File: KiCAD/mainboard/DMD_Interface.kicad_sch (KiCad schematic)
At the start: 21 parts, among them IC3 SN74AUP1G06DCKR, IC4 SN74AUP1G07DCKR, IC5 SN74AUP1G07DCKR, J1 AXT550124, J10 Conn_01x05_Pin, J30 Conn_01x08_Pin

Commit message: some new schematics
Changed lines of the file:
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@@
 	(rectangle
 		(start 17.145 58.42)
-		(end 104.775 167.005)
+		(end 104.775 185.42)
 		(stroke
 			(width 0)
@@
 		)
 		(instances
-			(project ""
+			(project "mainboard"
 				(path "/38e83f42-2cf9-4799-a46f-ca415d95b90a/2ef4843e-e813-4038-8f91-df837a4944f8"
 					(reference "J1")
@@
 		)
 		(instances
-			(project ""
+			(project "mainboard"
 				(path "/38e83f42-2cf9-4799-a46f-ca415d95b90a/2ef4843e-e813-4038-8f91-df837a4944f8"
 					(reference "D6")
@@
 		)
 		(instances
-			(project ""
+			(project "mainboard"
 				(path "/38e83f42-2cf9-4799-a46f-ca415d95b90a/2ef4843e-e813-4038-8f91-df837a4944f8"
 					(reference "IC4")
@@
 		)
 		(instances
-			(project ""
+			(project "mainboard"
 				(path "/38e83f42-2cf9-4799-a46f-ca415d95b90a/2ef4843e-e813-4038-8f91-df837a4944f8"
 					(reference "C116")
@@
 		)
 		(instances
-			(project ""
+			(project "mainboard"
 				(path "/38e83f42-2cf9-4799-a46f-ca415d95b90a/2ef4843e-e813-4038-8f91-df837a4944f8"
 					(reference "#PWR02")
@@
 		)
 		(instances
-			(project ""
+			(project "mainboard"
 				(path "/38e83f42-2cf9-4799-a46f-ca415d95b90a/2ef4843e-e813-4038-8f91-df837a4944f8"
 					(reference "IC3")
@@
 		)
 		(instances
-			(project ""
+			(project "mainboard"
 				(path "/38e83f42-2cf9-4799-a46f-ca415d95b90a/2ef4843e-e813-4038-8f91-df837a4944f8"
 					(reference "#PWR01")
@@
 		)
 		(instances
-			(project ""
+			(project "mainboard"
 				(path "/38e83f42-2cf9-4799-a46f-ca415d95b90a/2ef4843e-e813-4038-8f91-df837a4944f8"
 					(reference "J30")

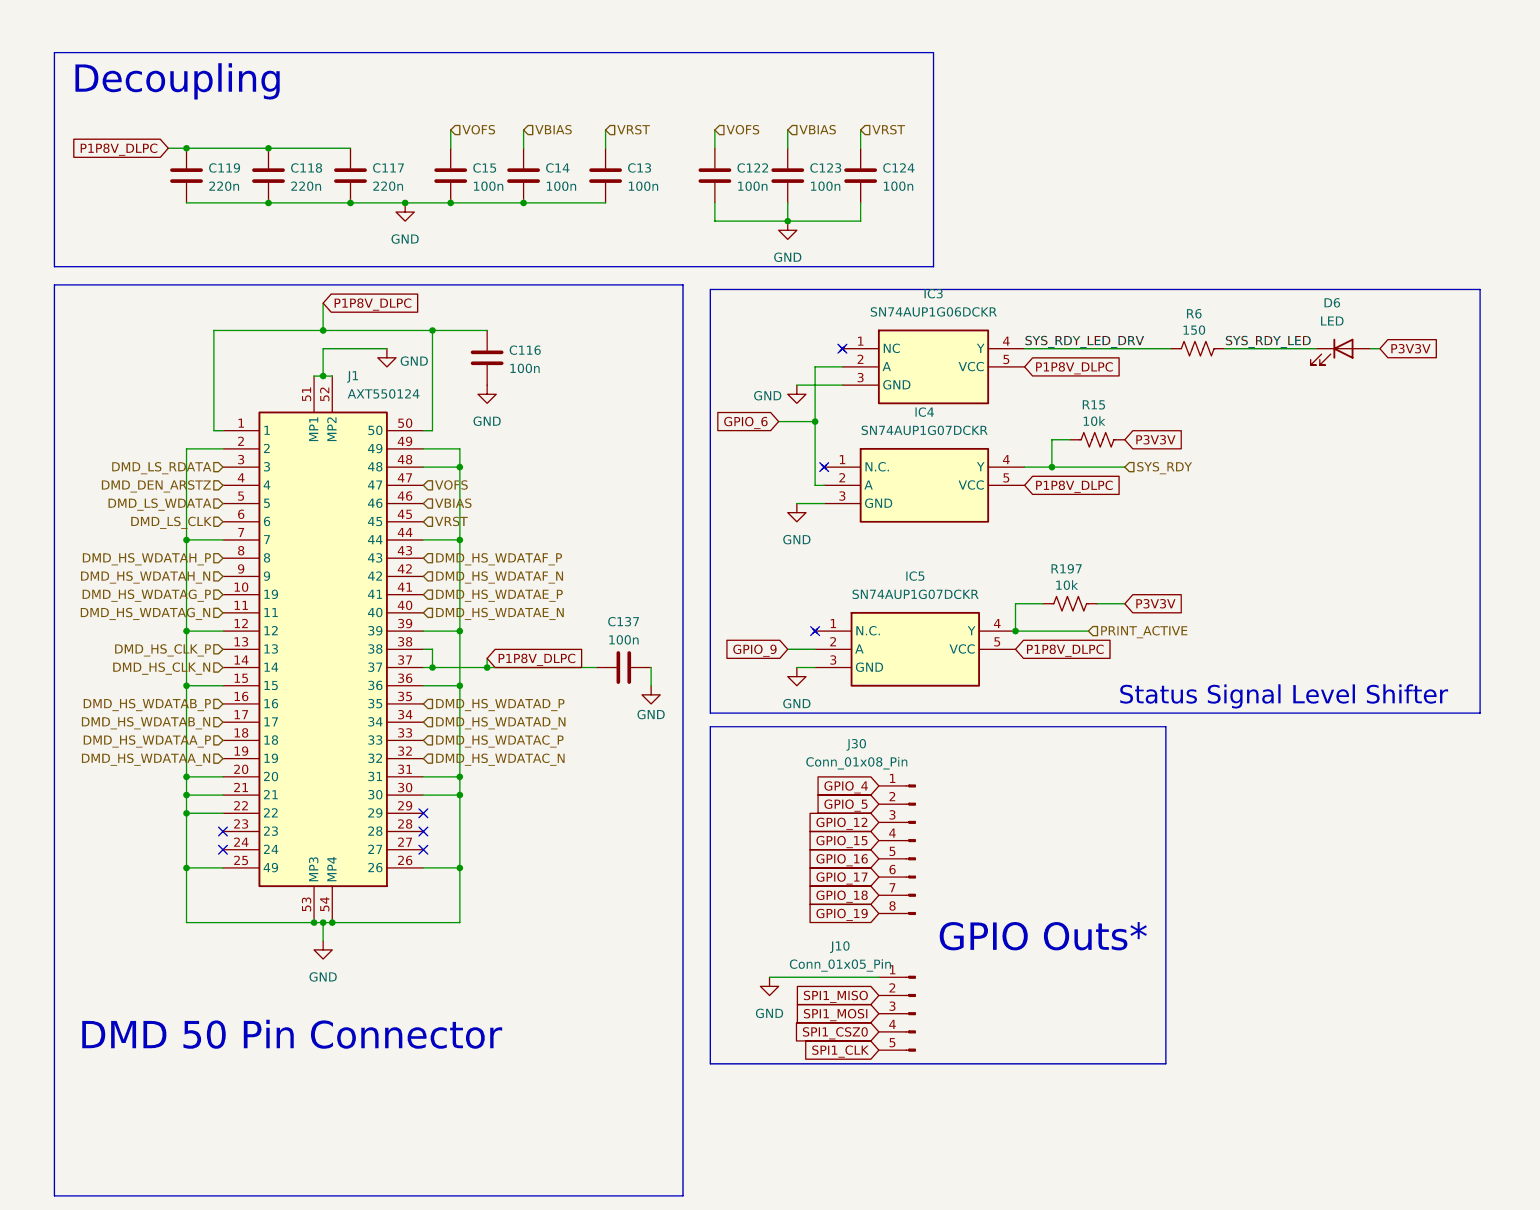
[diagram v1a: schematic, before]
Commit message: WIP dmd interface; made assembly for DMD, started new board for DMD interconnect
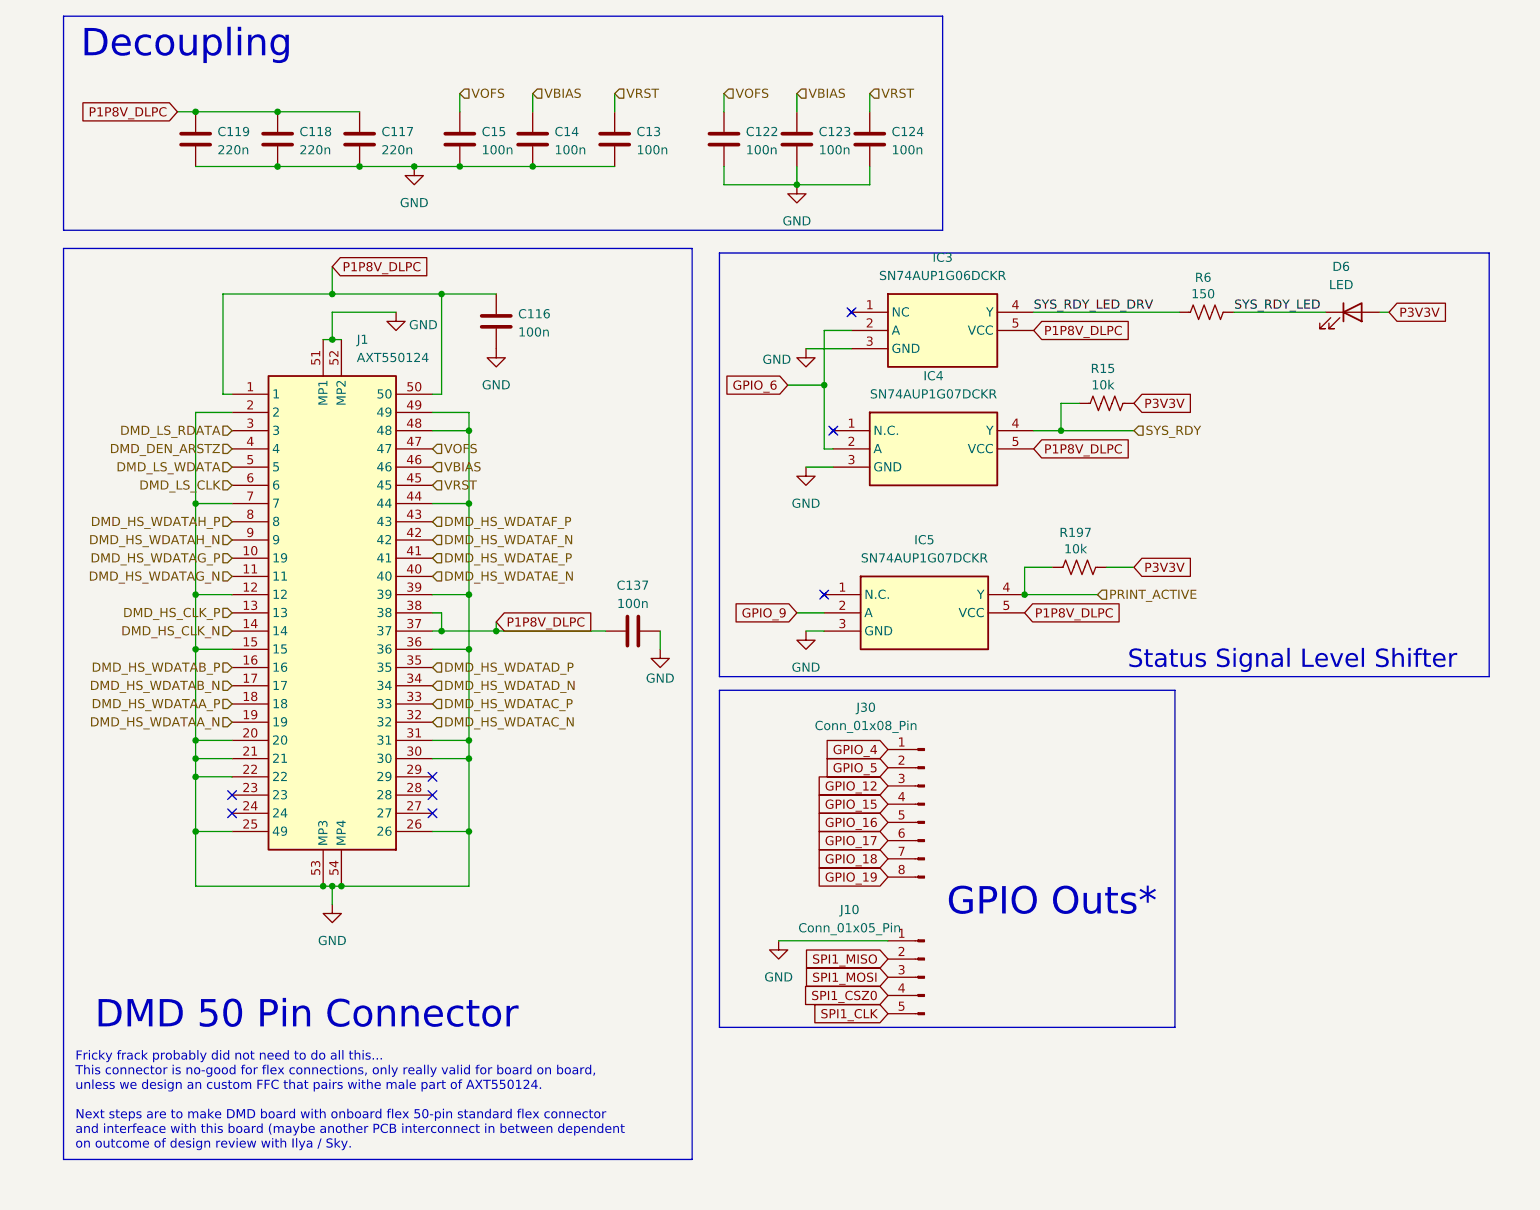
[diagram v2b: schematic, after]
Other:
- note added: "Fricky frack probably did not need to do all this... This connector is no-good for flex connections, only really valid for board on board, unless we design an custom FFC that pairs withe male part of AXT550124. Next steps are to make DMD board with onboard flex 50-pin standard flex connector and interfeace with this board (maybe another PCB interconnect in between dependent on outcome of design r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"
- moved on the sheet: C116, C117, C118, C119, C122, C123, C124, C13, C137, C14, C15, D6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

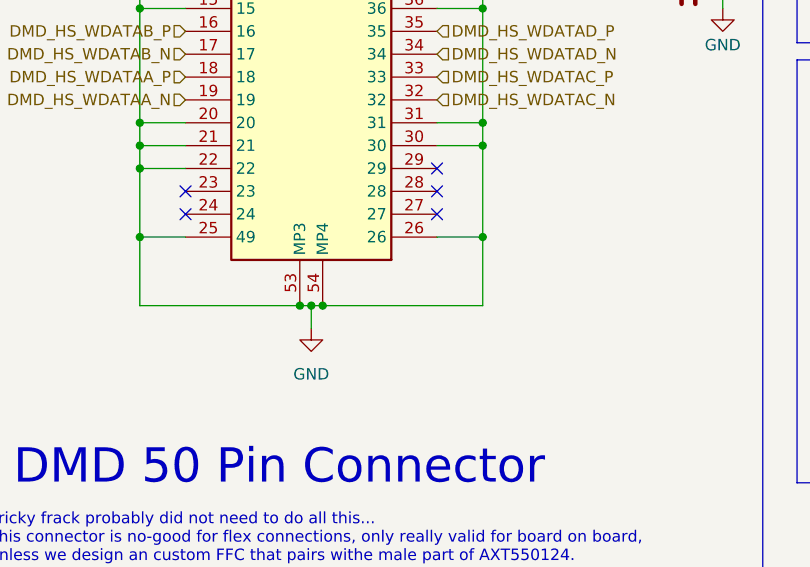
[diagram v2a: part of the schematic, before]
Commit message: assembly for lga footprint
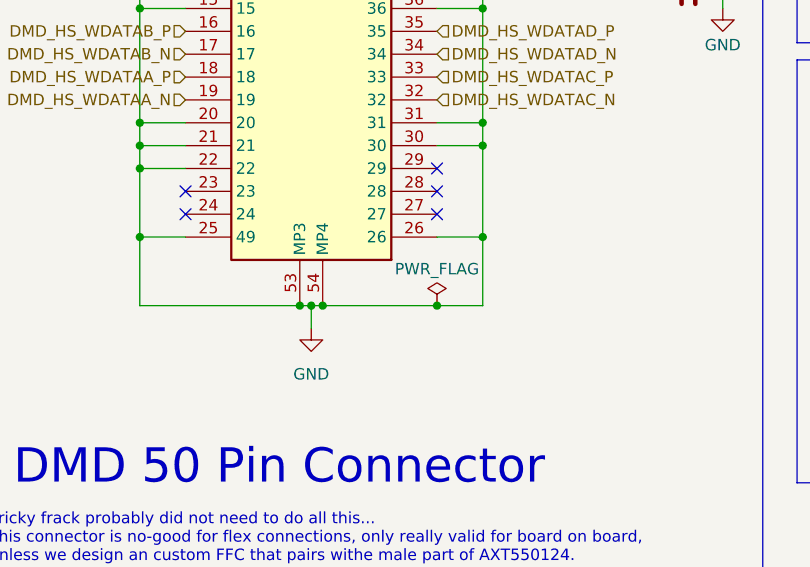
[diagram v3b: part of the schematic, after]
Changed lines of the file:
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@@
 	)
 	(junction
+		(at 69.85 142.24)
+		(diameter 0)
+		(color 0 0 0 0)
+	)
+	(junction
 		(at 74.93 134.62)
 		(diameter 0)
@@
 	(wire
 		(pts
+			(xy 69.85 142.24) (xy 74.93 142.24)
+		)
+		(stroke
+			(width 0)
+			(type default)
+		)
+	)
+	(wire
+		(pts
 			(xy 41.91 109.22) (xy 36.83 109.22)
 		)
@@
 	(wire
 		(pts
-			(xy 57.15 142.24) (xy 74.93 142.24)
+			(xy 57.15 142.24) (xy 69.85 142.24)
 		)
 		(stroke
@@
 					(unit 1)
 				)
+			)
+		)
+	)
+	(symbol
+		(lib_id "power:PWR_FLAG")
+		(at 69.85 142.24 0)
+		(unit 1)
+		(exclude_from_sim no)
+		(in_bom yes)
+		(on_board yes)
+		(dnp no)
+		(property "Reference" "#FLG01"
+			(at 69.85 140.335 0)
+			(effects
+				(font
+					(size 1.27 1.27)
+				)
+				(hide yes)
+			)
+		)
+		(property "Value" "PWR_FLAG"
+			(at 69.85 138.176 0)
+			(effects
+				(font
+					(size 1.27 1.27)
+				)
+			)
+		)
+		(property "Footprint" ""
+			(at 69.85 142.24 0)
+			(effects
+				(font
+					(size 1.27 1.27)
+				)
+				(hide yes)
+			)
+		)
+		(property "Datasheet" "~"
+			(at 69.85 142.24 0)
+			(effects
+				(font
+					(size 1.27 1.27)
+				)
+				(hide yes)
+			)
+		)
+		(property "Description" "Special symbol for telling ERC where power comes from"
+			(at 69.85 142.24 0)
+			(effects
+				(font
+					(size 1.27 1.27)
+				)
+				(hide yes)
+			)
+		)
+		(pin "1"
+		)
+		(instances
+			(project ""
+				(path "/38e83f42-2cf9-4799-a46f-ca415d95b90a/2ef4843e-e813-4038-8f91-df837a4944f8"
+					(reference "#FLG01")
+					(unit 1)
+				)

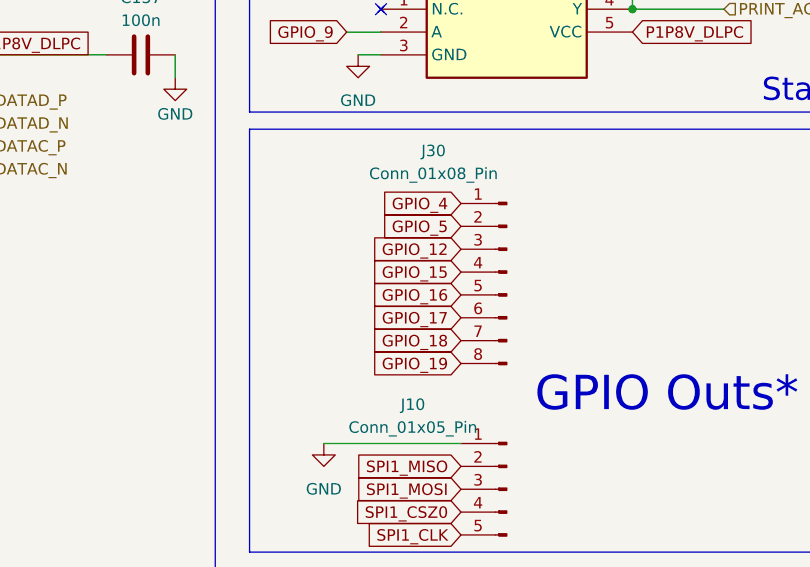
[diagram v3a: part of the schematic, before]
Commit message: gpios are now hierarchicals
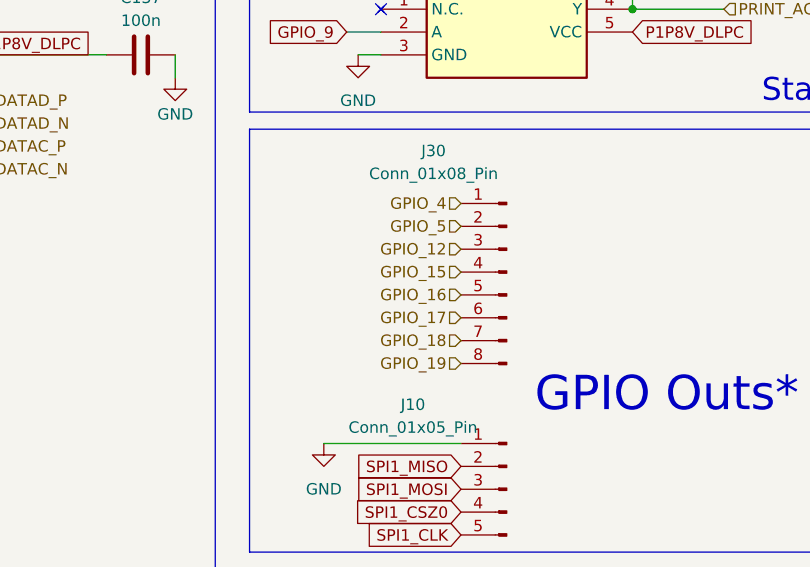
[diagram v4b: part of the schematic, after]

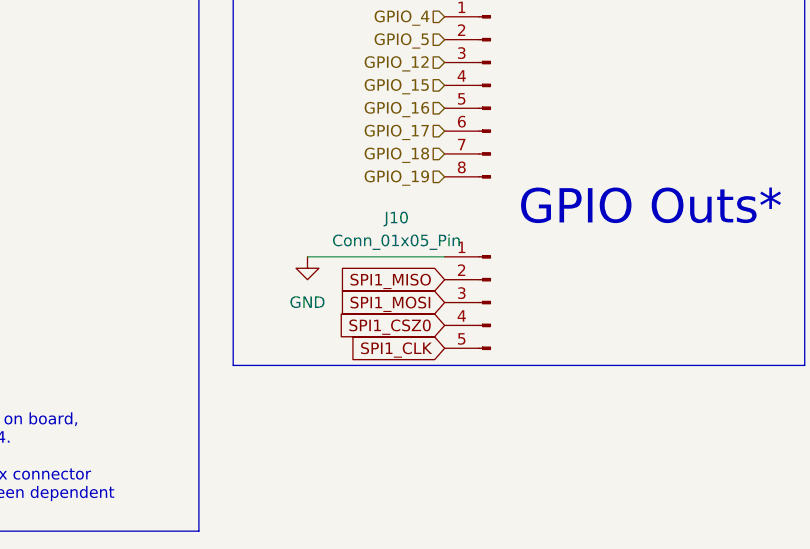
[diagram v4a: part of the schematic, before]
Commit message: fixed spi1 dlpc connections
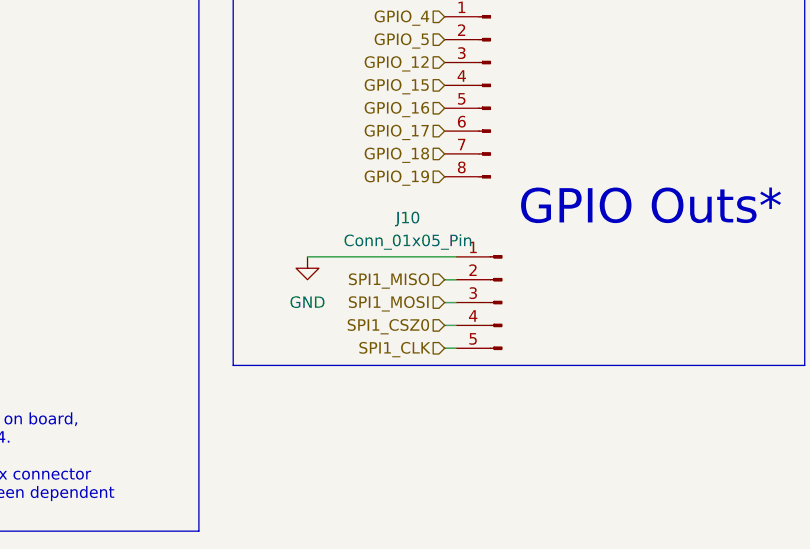
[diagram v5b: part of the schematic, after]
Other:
- moved on the sheet: J10
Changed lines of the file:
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@@
+	(wire
+		(pts
+			(xy 134.62 152.4) (xy 133.35 152.4)
+		)
+		(stroke
+			(width 0)
+			(type default)
+		)
+	)
+	(wire
+		(pts
+			(xy 134.62 154.94) (xy 133.35 154.94)
+		)
+		(stroke
+			(width 0)
+			(type default)
+		)
+	)
 	(wire
 		(pts
@@
 	(wire
 		(pts
+			(xy 134.62 160.02) (xy 133.35 160.02)
+		)
+		(stroke
+			(width 0)
+			(type default)
+		)
+	)
+	(wire
+		(pts
 			(xy 110.49 44.45) (xy 120.65 44.45)
 		)
@@
 	(wire
 		(pts
+			(xy 134.62 157.48) (xy 133.35 157.48)
+		)
+		(stroke
+			(width 0)
+			(type default)
+		)
+	)
+	(wire
+		(pts
 			(xy 152.4 101.6) (xy 162.56 101.6)
 		)
@@
 	(wire
 		(pts
-			(xy 133.35 149.86) (xy 118.11 149.86)
+			(xy 134.62 149.86) (xy 118.11 149.86)
 		)
 		(stroke
@@
 		)
 	)
-	(global_label "SPI1_CSZ0"
-		(shape input)
-		(at 133.35 157.48 180)
-		(fields_autoplaced yes)
-		(effects
-			(font
-				(size 1.27 1.27)
-			)
-			(justify right)
-		)
-		(property "Intersheetrefs" "${INTERSHEET_REFS}"
-			(at 120.2049 157.48 0)
-			(effects
-				(font
-					(size 1.27 1.27)
-				)
-				(justify right)
-				(hide yes)
-			)
-		)
-	)
 	(global_label "GPIO_9"
 		(shape input)
@@
 		)
 	)
-	(global_label "SPI1_MOSI"
-		(shape input)
-		(at 133.35 154.94 180)
-		(fields_autoplaced yes)
-		(effects
-			(font
-				(size 1.27 1.27)
-			)
-			(justify right)
-		)
-		(property "Intersheetrefs" "${INTERSHEET_REFS}"
-			(at 120.5072 154.94 0)
-			(effects
-				(font
-					(size 1.27 1.27)
-				)
-				(justify right)
-				(hide yes)
-			)
-		)
-	)
-	(global_label "SPI1_CLK"
-		(shape input)
-		(at 133.35 160.02 180)
-		(fields_autoplaced yes)
-		(effects
-			(font
-				(size 1.27 1.27)
-			)
-			(justify right)
-		)
-		(property "Intersheetrefs" "${INTERSHEET_REFS}"
-			(at 121.5353 160.02 0)
-			(effects
-				(font
-					(size 1.27 1.27)
-				)
-				(justify right)
-				(hide yes)
-			)
-		)
-	)
 	(global_label "P3V3V"
 		(shape input)
@@
 		)
 	)
-	(global_label "SPI1_MISO"
-		(shape input)
-		(at 133.35 152.4 180)
-		(fields_autoplaced yes)
-		(effects
-			(font
-				(size 1.27 1.27)
-			)
-			(justify right)
-		)
-		(property "Intersheetrefs" "${INTERSHEET_REFS}"
-			(at 120.5072 152.4 0)
-			(effects
-				(font
-					(size 1.27 1.27)
-				)
-				(justify right)
-				(hide yes)
-			)
-		)
-	)
 	(global_label "P1P8V_DLPC"
 		(shape input)
@@
 		)
 	)
+	(hierarchical_label "SPI1_MOSI"
+		(shape input)
+		(at 133.35 154.94 180)
+		(effects
+			(font
+				(size 1.27 1.27)
+			)
+			(justify right)
+		)
+	)
 	(hierarchical_label "VRST"
 		(shape input)
@@
 		)
 	)
+	(hierarchical_label "SPI1_CLK"
+		(shape input)
+		(at 133.35 160.02 180)
+		(effects
+			(font
+				(size 1.27 1.27)
+			)
+			(justify right)
+		)
+	)
 	(hierarchical_label "DMD_HS_WDATAA_N"
 		(shape input)
@@
 		)
 	)
+	(hierarchical_label "SPI1_CSZ0"
+		(shape input)
+		(at 133.35 157.48 180)
+		(effects
+			(font
+				(size 1.27 1.27)
+			)
+			(justify right)
+		)
+	)
 	(hierarchical_label "PRINT_ACTIVE"
 		(shape input)
@@
 		(shape input)
 		(at 41.91 86.36 180)
+		(effects
+			(font
+				(size 1.27 1.27)
+			)
+			(justify right)
+		)
+	)
+	(hierarchical_label "SPI1_MISO"
+		(shape input)
+		(at 133.35 152.4 180)
 		(effects
 			(font
@@
 	(symbol
 		(lib_id "Connector:Conn_01x05_Pin")
-		(at 138.43 154.94 0)
+		(at 139.7 154.94 0)
 		(mirror y)
 		(unit 1)
@@
 		(dnp no)
 		(property "Reference" "J10"
-			(at 128.016 145.542 0)
+			(at 129.286 145.542 0)
 			(effects
 				(font
@@
 		)
 		(property "Value" "Conn_01x05_Pin"
-			(at 128.016 148.082 0)
+			(at 129.286 148.082 0)
 			(effects
 				(font
@@
 		)
 		(property "Footprint" "Connector_PinHeader_2.54mm:PinHeader_1x05_P2.54mm_Vertical"
-			(at 138.43 154.94 0)
+			(at 139.7 154.94 0)
 			(effects
 				(font
@@
 		)
 		(property "Datasheet" "~"
-			(at 138.43 154.94 0)
+			(at 139.7 154.94 0)
 			(effects
 				(font
@@
 		)
 		(property "Description" "Generic connector, single row, 01x05, script generated"
-			(at 138.43 154.94 0)
-			(effects
-				(font
+			(at 139.7 154.94 0)
+			(effects
+				(font
